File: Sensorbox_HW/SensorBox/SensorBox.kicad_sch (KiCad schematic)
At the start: 81 parts, among them U1 BME280, U11 PS1-O3-100, U12 DS3231M, U13 OPA197xD, U2 OPA197xD, U4 MC33063AD, U5 OPA197xD, U6 MAX31855EASA, U8 HPP845E131R5

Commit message: Doku V3
Die Dokumentation bezüglich der 3.Version von der Hardware wurde geschrieben.

Co-Authored-By: God <120719507+Mcy61@users.noreply.github.com>
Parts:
- CT1: value 1500pF -> 1500pF - 50V
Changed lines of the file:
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@@
 			)
 		)
-		(property "Value" "1500pF"
+		(property "Value" "1500pF - 50V"
 			(at 53.34 55.8799 0)
 			(effects

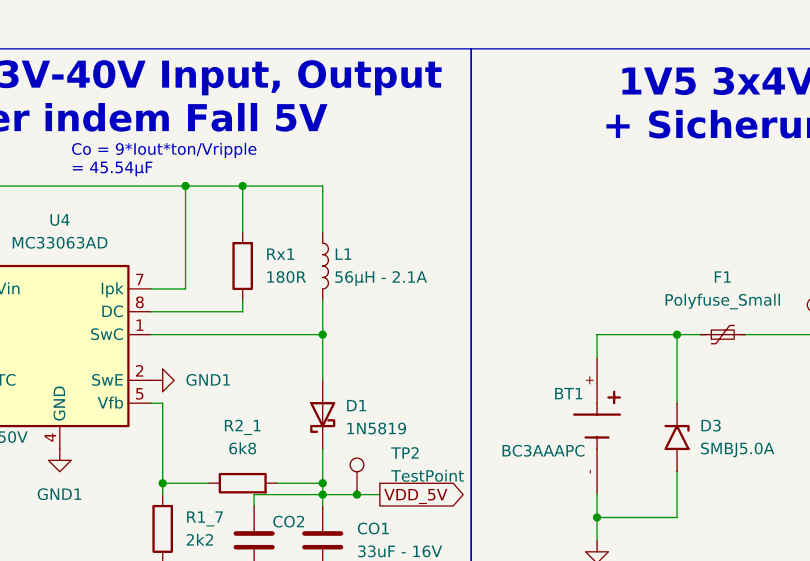
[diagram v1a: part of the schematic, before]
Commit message: Layout, Schaltplan, Doku
Footprint von L1 abgeändert, Doku weitergearbeitet
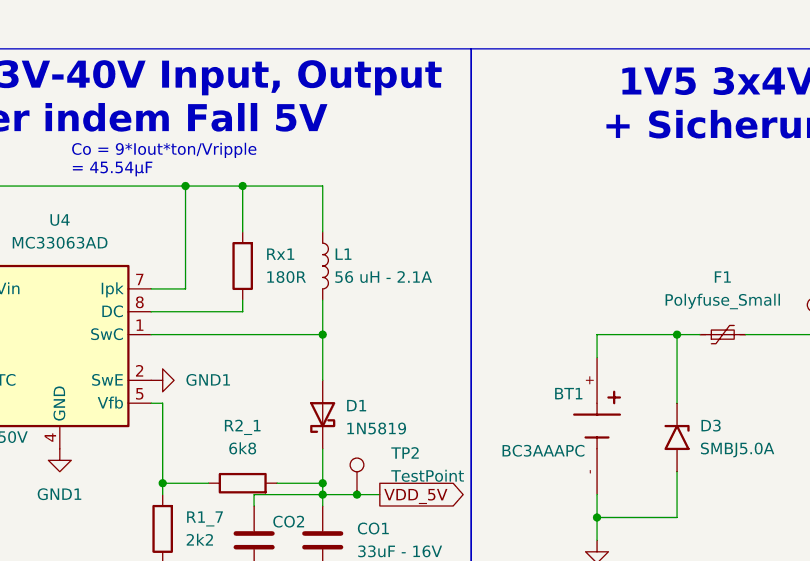
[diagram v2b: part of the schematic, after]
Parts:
- L1: value 56µH - 2.1A -> 56 uH - 2.1A; footprint Inductor_SMD:L_0805_2012Metric_Pad1.05x1.20mm_HandSolder -> L1_Spule:L1
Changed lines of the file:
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@@
-	)
-	(symbol
-		(lib_id "Device:L")
-		(at 97.79 36.83 0)
-		(unit 1)
-		(exclude_from_sim no)
-		(in_bom yes)
-		(on_board yes)
-		(dnp no)
-		(fields_autoplaced yes)
-		(property "Reference" "L1"
-			(at 99.06 35.5599 0)
-			(effects
-				(font
-					(size 1.27 1.27)
-				)
-				(justify left)
-			)
-		)
-		(property "Value" "56µH - 2.1A"
-			(at 99.06 38.0999 0)
-			(effects
-				(font
-					(size 1.27 1.27)
-				)
-				(justify left)
-			)
-		)
-		(property "Footprint" "Inductor_SMD:L_0805_2012Metric_Pad1.05x1.20mm_HandSolder"
-			(at 97.79 36.83 0)
-			(effects
-				(font
-					(size 1.27 1.27)
-				)
-				(hide yes)
-			)
-		)
-		(property "Datasheet" "~"
-			(at 97.79 36.83 0)
-			(effects
-				(font
-					(size 1.27 1.27)
-				)
-				(hide yes)
-			)
-		)
-		(property "Description" "Inductor"
-			(at 97.79 36.83 0)
-			(effects
-				(font
-					(size 1.27 1.27)
-				)
-				(hide yes)
-			)
-		)
-		(pin "2"
-		)
-		(pin "1"
-		)
-		(instances
-			(project "SensorBox"
-				(path "/7cbe8151-7294-42e6-9c4e-6ec8952d674f"
-					(reference "L1")
-					(unit 1)
-				)
-			)
-		)
 	)
 	(symbol
@@
 					(unit 1)
 				)
+			)
+		)
+	)
+	(symbol
+		(lib_id "Device:L")
+		(at 97.79 36.83 0)
+		(unit 1)
+		(exclude_from_sim no)
+		(in_bom yes)
+		(on_board yes)
+		(dnp no)
+		(fields_autoplaced yes)
+		(property "Reference" "L1"
+			(at 99.06 35.5599 0)
+			(effects
+				(font
+					(size 1.27 1.27)
+				)
+				(justify left)
+			)
+		)
+		(property "Value" "56 uH - 2.1A"
+			(at 99.06 38.0999 0)
+			(effects
+				(font
+					(size 1.27 1.27)
+				)
+				(justify left)
+			)
+		)
+		(property "Footprint" "L1_Spule:L1"
+			(at 97.79 36.83 0)
+			(effects
+				(font
+					(size 1.27 1.27)
+				)
+				(hide yes)
+			)
+		)
+		(property "Datasheet" "~"
+			(at 97.79 36.83 0)
+			(effects
+				(font
+					(size 1.27 1.27)
+				)
+				(hide yes)
+			)
+		)
+		(property "Description" "Inductor"
+			(at 97.79 36.83 0)
+			(effects
+				(font
+					(size 1.27 1.27)
+				)
+				(hide yes)
+			)
+		)
+		(pin "2"
+		)
+		(pin "1"
+		)
+		(instances
+			(project ""
+				(path "/7cbe8151-7294-42e6-9c4e-6ec8952d674f"
+					(reference "L1")
+					(unit 1)
+				)

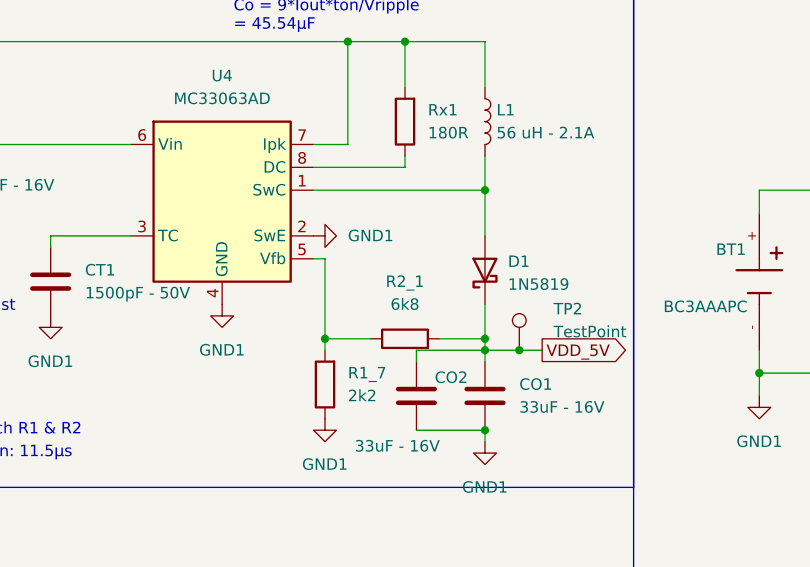
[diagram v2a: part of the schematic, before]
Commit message: Wiederstand bei Spannungsregler dazugeschalten
Parallel zu R2_1
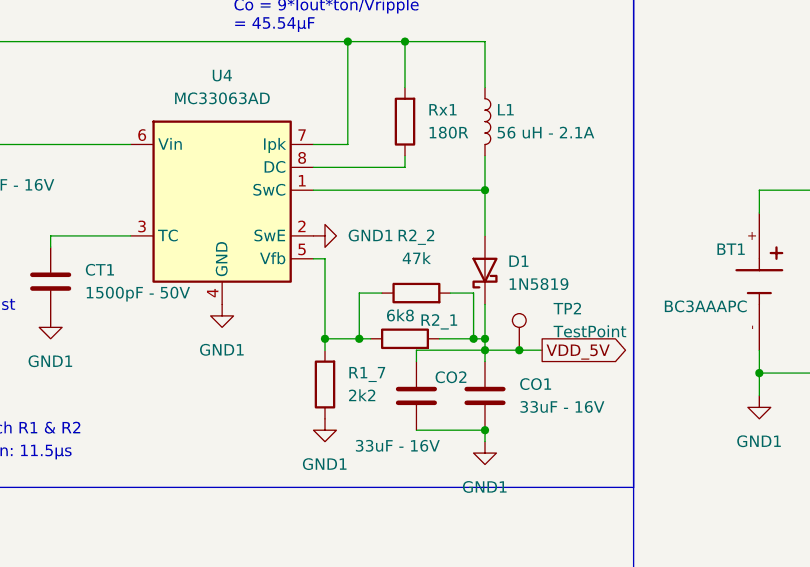
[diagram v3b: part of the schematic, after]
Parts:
- added R2_2: 47k, Resistor_SMD:R_1206_3216Metric_Pad1.30x1.75mm_HandSolder, symbol Device:R
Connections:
- net VDD_5V: now also R2_2.2
- net at R1_7.2, R2_1.1, U4.5 (Vfb): now also R2_2.1
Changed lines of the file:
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@@
 	)
 	(junction
+		(at 96.52 60.96)
+		(diameter 0)
+		(color 0 0 0 0)
+	)
+	(junction
 		(at 128.27 64.77)
 		(diameter 0)
@@
 	)
 	(junction
+		(at 83.82 60.96)
+		(diameter 0)
+		(color 0 0 0 0)
+	)
+	(junction
 		(at 109.22 246.38)
 		(diameter 0)
@@
 	(wire
 		(pts
-			(xy 92.71 60.96) (xy 97.79 60.96)
+			(xy 92.71 60.96) (xy 96.52 60.96)
 		)
 		(stroke
@@
 	(wire
 		(pts
+			(xy 96.52 60.96) (xy 97.79 60.96)
+		)
+		(stroke
+			(width 0)
+			(type default)
+		)
+	)
+	(wire
+		(pts
 			(xy 80.01 60.96) (xy 80.01 62.23)
 		)
@@
 	(wire
 		(pts
+			(xy 93.98 55.88) (xy 96.52 55.88)
+		)
+		(stroke
+			(width 0)
+			(type default)
+		)
+	)
+	(wire
+		(pts
 			(xy 44.45 205.74) (xy 44.45 210.82)
 		)
@@
 	(wire
 		(pts
+			(xy 83.82 60.96) (xy 85.09 60.96)
+		)
+		(stroke
+			(width 0)
+			(type default)
+		)
+	)
+	(wire
+		(pts
 			(xy 316.23 190.5) (xy 314.96 190.5)
 		)
@@
 	(wire
 		(pts
+			(xy 86.36 55.88) (xy 83.82 55.88)
+		)
+		(stroke
+			(width 0)
+			(type default)
+		)
+	)
+	(wire
+		(pts
 			(xy 381 129.54) (xy 381 132.08)
 		)
@@
 	(wire
 		(pts
+			(xy 83.82 55.88) (xy 83.82 60.96)
+		)
+		(stroke
+			(width 0)
+			(type default)
+		)
+	)
+	(wire
+		(pts
 			(xy 88.9 41.91) (xy 88.9 40.64)
 		)
@@
 	(wire
 		(pts
-			(xy 80.01 60.96) (xy 85.09 60.96)
+			(xy 80.01 60.96) (xy 83.82 60.96)
 		)
 		(stroke
@@
 	(wire
 		(pts
+			(xy 96.52 55.88) (xy 96.52 60.96)
+		)
+		(stroke
+			(width 0)
+			(type default)
+		)
+	)
+	(wire
+		(pts
 			(xy 372.11 26.67) (xy 372.11 27.94)
 		)
@@
 	)
 	(symbol
+		(lib_id "Device:R")
+		(at 90.17 55.88 90)
+		(unit 1)
+		(exclude_from_sim no)
+		(in_bom yes)
+		(on_board yes)
+		(dnp no)
+		(fields_autoplaced yes)
+		(property "Reference" "R2_2"
+			(at 90.17 49.53 90)
+			(effects
+				(font
+					(size 1.27 1.27)
+				)
+			)
+		)
+		(property "Value" "47k"
+			(at 90.17 52.07 90)
+			(effects
+				(font
+					(size 1.27 1.27)
+				)
+			)
+		)
+		(property "Footprint" "Resistor_SMD:R_1206_3216Metric_Pad1.30x1.75mm_HandSolder"
+			(at 90.17 57.658 90)
+			(effects
+				(font
+					(size 1.27 1.27)
+				)
+				(hide yes)
+			)
+		)
+		(property "Datasheet" "~"
+			(at 90.17 55.88 0)
+			(effects
+				(font
+					(size 1.27 1.27)
+				)
+				(hide yes)
+			)
+		)
+		(property "Description" "Resistor"
+			(at 90.17 55.88 0)
+			(effects
+				(font
+					(size 1.27 1.27)
+				)
+				(hide yes)
+			)
+		)
+		(pin "1"
+		)
+		(pin "2"
+		)
+		(instances
+			(project "SensorBox"
+				(path "/7cbe8151-7294-42e6-9c4e-6ec8952d674f"
+					(reference "R2_2")
+					(unit 1)
+				)
+			)
+		)
+	)
+	(symbol
 		(lib_id "power:GND1")
 		(at 78.74 49.53 90)
@@
 		(on_board yes)
 		(dnp no)
-		(fields_autoplaced yes)
 		(property "Reference" "R2_1"
-			(at 88.9 54.61 90)
+			(at 92.71 58.928 90)
 			(effects
 				(font
@@
 		)
 		(property "Value" "6k8"
-			(at 88.9 57.15 90)
+			(at 88.392 58.42 90)
 			(effects
 				(font

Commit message: Finales Layout angefangen
.
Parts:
- removed TP5, TP6, TP7: TestPoint, TestPoint:TestPoint_Loop_D1.80mm_Drill1.0mm_Beaded, symbol Connector:TestPoint
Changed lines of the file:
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@@
 	)
 	(junction
-		(at 294.64 34.29)
-		(diameter 0)
-		(color 0 0 0 0)
-	)
-	(junction
 		(at 52.07 143.51)
 		(diameter 0)
@@
 	)
 	(junction
-		(at 294.64 31.75)
-		(diameter 0)
-		(color 0 0 0 0)
-	)
-	(junction
 		(at 36.83 166.37)
 		(diameter 0)
@@
 	(wire
 		(pts
-			(xy 294.64 31.75) (xy 297.18 31.75)
+			(xy 281.94 31.75) (xy 297.18 31.75)
 		)
 		(stroke
@@
 	(wire
 		(pts
-			(xy 294.64 34.29) (xy 297.18 34.29)
+			(xy 281.94 34.29) (xy 297.18 34.29)
 		)
 		(stroke
@@
 	(wire
 		(pts
-			(xy 281.94 31.75) (xy 294.64 31.75)
-		)
-		(stroke
-			(width 0)
-			(type default)
-		)
-	)
-	(wire
-		(pts
 			(xy 378.46 99.06) (xy 378.46 88.9)
 		)
@@
 	(wire
 		(pts
-			(xy 281.94 34.29) (xy 294.64 34.29)
-		)
-		(stroke
-			(width 0)
-			(type default)
-		)
-	)
-	(wire
-		(pts
 			(xy 41.91 156.21) (xy 41.91 158.75)
 		)
@@
 	)
 	(symbol
-		(lib_id "Connector:TestPoint")
-		(at 294.64 31.75 0)
-		(unit 1)
-		(exclude_from_sim no)
-		(in_bom yes)
-		(on_board yes)
-		(dnp no)
-		(fields_autoplaced yes)
-		(property "Reference" "TP5"
-			(at 298.45 27.1779 0)
-			(effects
-				(font
-					(size 1.27 1.27)
-				)
-				(justify left)
-			)
-		)
-		(property "Value" "TestPoint"
-			(at 298.45 29.7179 0)
-			(effects
-				(font
-					(size 1.27 1.27)
-				)
-				(justify left)
-			)
-		)
-		(property "Footprint" "TestPoint:TestPoint_Loop_D1.80mm_Drill1.0mm_Beaded"
-			(at 299.72 31.75 0)
-			(effects
-				(font
-					(size 1.27 1.27)
-				)
-				(hide yes)
-			)
-		)
-		(property "Datasheet" "~"
-			(at 299.72 31.75 0)
-			(effects
-				(font
-					(size 1.27 1.27)
-				)
-				(hide yes)
-			)
-		)
-		(property "Description" "test point"
-			(at 294.64 31.75 0)
-			(effects
-				(font
-					(size 1.27 1.27)
-				)
-				(hide yes)
-			)
-		)
-		(pin "1"
-		)
-		(instances
-			(project "SensorBox"
-				(path "/7cbe8151-7294-42e6-9c4e-6ec8952d674f"
-					(reference "TP5")
-					(unit 1)
-				)
-			)
-		)
-	)
-	(symbol
 		(lib_id "Device:R")
 		(at 25.4 215.9 180)
@@
 	)
 	(symbol
-		(lib_id "Connector:TestPoint")
-		(at 375.92 43.18 0)
-		(unit 1)
-		(exclude_from_sim no)
-		(in_bom yes)
-		(on_board yes)
-		(dnp no)
-		(fields_autoplaced yes)
-		(property "Reference" "TP7"
-			(at 379.73 38.6079 0)
-			(effects
-				(font
-					(size 1.27 1.27)
-				)
-				(justify left)
-			)
-		)
-		(property "Value" "TestPoint"
-			(at 379.73 41.1479 0)
-			(effects
-				(font
-					(size 1.27 1.27)
-				)
-				(justify left)
-			)
-		)
-		(property "Footprint" "TestPoint:TestPoint_Loop_D1.80mm_Drill1.0mm_Beaded"
-			(at 381 43.18 0)
-			(effects
-				(font
-					(size 1.27 1.27)
-				)
-				(hide yes)
-			)
-		)
-		(property "Datasheet" "~"
-			(at 381 43.18 0)
-			(effects
-				(font
-					(size 1.27 1.27)
-				)
-				(hide yes)
-			)
-		)
-		(property "Description" "test point"
-			(at 375.92 43.18 0)
-			(effects
-				(font
-					(size 1.27 1.27)
-				)
-				(hide yes)
-			)
-		)
-		(pin "1"
-		)
-		(instances
-			(project "SensorBox"
-				(path "/7cbe8151-7294-42e6-9c4e-6ec8952d674f"
-					(reference "TP7")
-					(unit 1)
-				)
-			)
-		)
-	)
-	(symbol
 		(lib_id "Device:C")
 		(at 375.92 19.05 180)
@@
 					(unit 1)
 				)
-			)
-		)
-	)
-	(symbol
-		(lib_id "Connector:TestPoint")
-		(at 294.64 34.29 180)
-		(unit 1)
-		(exclude_from_sim no)
-		(in_bom yes)
-		(on_board yes)
-		(dnp no)
-		(fields_autoplaced yes)
-		(property "Reference" "TP6"
-			(at 297.18 36.3219 0)
-			(effects
-				(font
-					(size 1.27 1.27)
-				)
-				(justify right)
-			)
-		)
-		(property "Value" "TestPoint"
-			(at 297.18 38.8619 0)
-			(effects
-				(font
-					(size 1.27 1.27)
-				)
-				(justify right)
-			)
-		)
-		(property "Footprint" "TestPoint:TestPoint_Loop_D1.80mm_Drill1.0mm_Beaded"
-			(at 289.56 34.29 0)
-			(effects
-				(font
-					(size 1.27 1.27)
-				)
-				(hide yes)
-			)
-		)
-		(property "Datasheet" "~"
-			(at 289.56 34.29 0)
-			(effects
-				(font
-					(size 1.27 1.27)
-				)
-				(hide yes)
-			)
-		)
-		(property "Description" "test point"
-			(at 294.64 34.29 0)
-			(effects
-				(font
-					(size 1.27 1.27)
-				)
-				(hide yes)
-			)
-		)
-		(pin "1"
-		)
-		(instances
-			(project "SensorBox"
-				(path "/7cbe8151-7294-42e6-9c4e-6ec8952d674f"
-					(reference "TP6")
-					(unit 1)
-				)

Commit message: Layout
Layout komplett neugemacht (Sensoren usw. besser platziert.)
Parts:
- added S1, S2: ATE1D-2M3-10-Z, Schalter_neu:SW_ATE1D-2M3-10-Z, symbol Schalter_neu:ATE1D-2M3-10-Z
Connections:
- net VCC_Bat: now also S1.1; no longer F1.2
- net VDD_5V: now also S2.2; no longer U7.19 (5V)
- new net: F1.2, S1.2
- new net: S2.1, U7.19 (5V)
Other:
- moved on the sheet: F1, TP3

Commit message: Schalter2-Änderungen
Schalter zwischen 2 GPIOs hinzugefügt
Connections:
- net VDD_5V: now also U7.19 (5V); no longer S2.2
- net at S2.1: no longer U7.19 (5V)
- net at S2.3: now also U7.6 (35)
- net at U7.7 (32): now also S2.2
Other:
- moved on the sheet: S2
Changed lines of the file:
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@@
 	(wire
 		(pts
+			(xy 222.25 40.64) (xy 222.25 44.45)
+		)
+		(stroke
+			(width 0)
+			(type default)
+		)
+	)
+	(wire
+		(pts
 			(xy 271.78 190.5) (xy 273.05 190.5)
 		)
@@
 	(wire
 		(pts
-			(xy 191.77 248.92) (xy 195.58 248.92)
+			(xy 222.25 44.45) (xy 256.54 44.45)
 		)
 		(stroke
@@
 	(wire
 		(pts
-			(xy 151.13 259.08) (xy 151.13 265.43)
+			(xy 191.77 248.92) (xy 195.58 248.92)
 		)
 		(stroke
@@
 	(wire
 		(pts
-			(xy 151.13 265.43) (xy 157.48 265.43)
+			(xy 151.13 259.08) (xy 151.13 265.43)
 		)
 		(stroke
@@
 	(wire
 		(pts
-			(xy 184.15 237.49) (xy 191.77 237.49)
+			(xy 151.13 265.43) (xy 157.48 265.43)
 		)
 		(stroke
@@
 	(wire
 		(pts
-			(xy 281.94 44.45) (xy 285.75 44.45)
+			(xy 184.15 237.49) (xy 191.77 237.49)
 		)
 		(stroke
@@
 	(wire
 		(pts
-			(xy 246.38 72.39) (xy 246.38 74.93)
+			(xy 281.94 44.45) (xy 285.75 44.45)
 		)
 		(stroke
@@
 	(wire
 		(pts
+			(xy 256.54 41.91) (xy 237.49 41.91)
+		)
+		(stroke
+			(width 0)
+			(type default)
+		)
+	)
+	(wire
+		(pts
 			(xy 171.45 237.49) (xy 171.45 259.08)
 		)
@@
 	(wire
 		(pts
+			(xy 237.49 41.91) (xy 237.49 43.18)
+		)
+		(stroke
+			(width 0)
+			(type default)
+		)
+	)
+	(wire
+		(pts
 			(xy 370.84 104.14) (xy 386.08 104.14)
 		)
@@
 	(wire
 		(pts
-			(xy 228.6 74.93) (xy 231.14 74.93)
-		)
-		(stroke
-			(width 0)
-			(type default)
-		)
-	)
-	(wire
-		(pts
 			(xy 250.19 46.99) (xy 256.54 46.99)
 		)
@@
 	(wire
 		(pts
+			(xy 250.19 74.93) (xy 256.54 74.93)
+		)
+		(stroke
+			(width 0)
+			(type default)
+		)
+	)
+	(wire
+		(pts
 			(xy 359.41 24.13) (xy 359.41 30.48)
 		)
@@
 	(wire
 		(pts
-			(xy 246.38 74.93) (xy 256.54 74.93)
-		)
-		(stroke
-			(width 0)
-			(type default)
-		)
-	)
-	(wire
-		(pts
 			(xy 41.91 210.82) (xy 44.45 210.82)
 		)
@@
 	(global_label "VDD_5V"
 		(shape input)
-		(at 228.6 74.93 180)
+		(at 250.19 74.93 180)
 		(fields_autoplaced yes)
 		(effects
@@
 		)
 		(property "Intersheetrefs" "${INTERSHEET_REFS}"
-			(at 218.7205 74.93 0)
+			(at 240.3105 74.93 0)
 			(effects
 				(font
@@
 	(symbol
 		(lib_id "Schalter_neu:ATE1D-2M3-10-Z")
-		(at 238.76 74.93 0)
+		(at 229.87 40.64 0)
 		(unit 1)
 		(exclude_from_sim no)
@@
 		(fields_autoplaced yes)
 		(property "Reference" "S2"
-			(at 238.76 67.31 0)
+			(at 229.87 33.02 0)
 			(effects
 				(font
@@
 		)
 		(property "Value" "ATE1D-2M3-10-Z"
-			(at 238.76 69.85 0)
+			(at 229.87 35.56 0)
 			(effects
 				(font
@@
 		)
 		(property "Footprint" "Schalter_neu:SW_ATE1D-2M3-10-Z"
-			(at 238.76 74.93 0)
+			(at 229.87 40.64 0)
 			(effects
 				(font
@@
 		)
 		(property "Datasheet" ""
-			(at 238.76 74.93 0)
+			(at 229.87 40.64 0)
 			(effects
 				(font
@@
 		)
 		(property "Description" ""
-			(at 238.76 74.93 0)
+			(at 229.87 40.64 0)
 			(effects
 				(font
@@
 		)
 		(property "MF" ""
-			(at 238.76 74.93 0)
+			(at 229.87 40.64 0)
 			(effects
 				(font
@@
 		)
 		(property "MAXIMUM_PACKAGE_HEIGHT" ""
-			(at 238.76 74.93 0)
+			(at 229.87 40.64 0)
 			(effects
 				(font
@@
 		)
 		(property "Package" ""
-			(at 238.76 74.93 0)
+			(at 229.87 40.64 0)
 			(effects
 				(font
@@
 		)
 		(property "Price" ""
-			(at 238.76 74.93 0)
+			(at 229.87 40.64 0)
 			(effects
 				(font
@@
 		)
 		(property "Check_prices" ""
-			(at 238.76 74.93 0)
+			(at 229.87 40.64 0)
 			(effects
 				(font
@@
 		)
 		(property "STANDARD" ""
-			(at 238.76 74.93 0)
+			(at 229.87 40.64 0)
 			(effects
 				(font
@@
 		)
 		(property "PARTREV" ""
-			(at 238.76 74.93 0)
+			(at 229.87 40.64 0)
 			(effects
 				(font
@@
 		)
 		(property "SnapEDA_Link" ""
-			(at 238.76 74.93 0)
+			(at 229.87 40.64 0)
 			(effects
 				(font
@@
 		)
 		(property "MP" ""
-			(at 238.76 74.93 0)
+			(at 229.87 40.64 0)
 			(effects
 				(font
@@
 		)
 		(property "Description_1" ""
-			(at 238.76 74.93 0)
+			(at 229.87 40.64 0)
 			(effects
 				(font
@@
 		)
 		(property "Availability" ""
-			(at 238.76 74.93 0)
+			(at 229.87 40.64 0)
 			(effects
 				(font
@@
 		)
 		(property "MANUFACTURER" ""
-			(at 238.76 74.93 0)
+			(at 229.87 40.64 0)
 			(effects
 				(font
